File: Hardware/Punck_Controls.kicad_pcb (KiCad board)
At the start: 2 copper layers, 91.2 x 110 mm, 36 parts, among them J1 Conn_01x12_Female, J10 Kick_In, J11 USB_B_Micro, J12 Tempo_Out, J13 Audio_Out_L, J14 Audio_Out_R, J15 Midi_In, J2 Conn_01x12_Female, J3 Conn_01x12_Female, J4 Conn_01x12_Female, J5 Snare_In, J6 CH_In, J7 OH_In, J8 SamplerA_In, J9 SamplerB_In

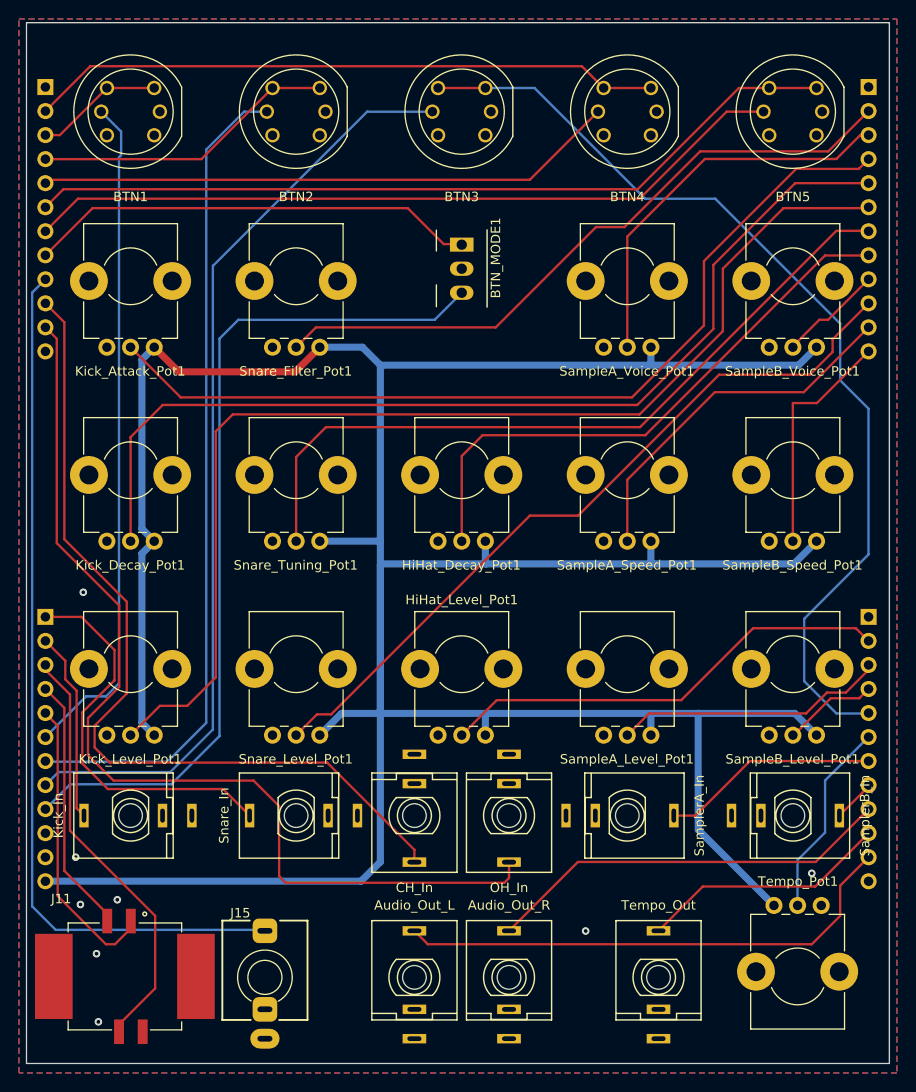
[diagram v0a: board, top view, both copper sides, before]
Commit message: Added test code to use PWM control on voice LEDs
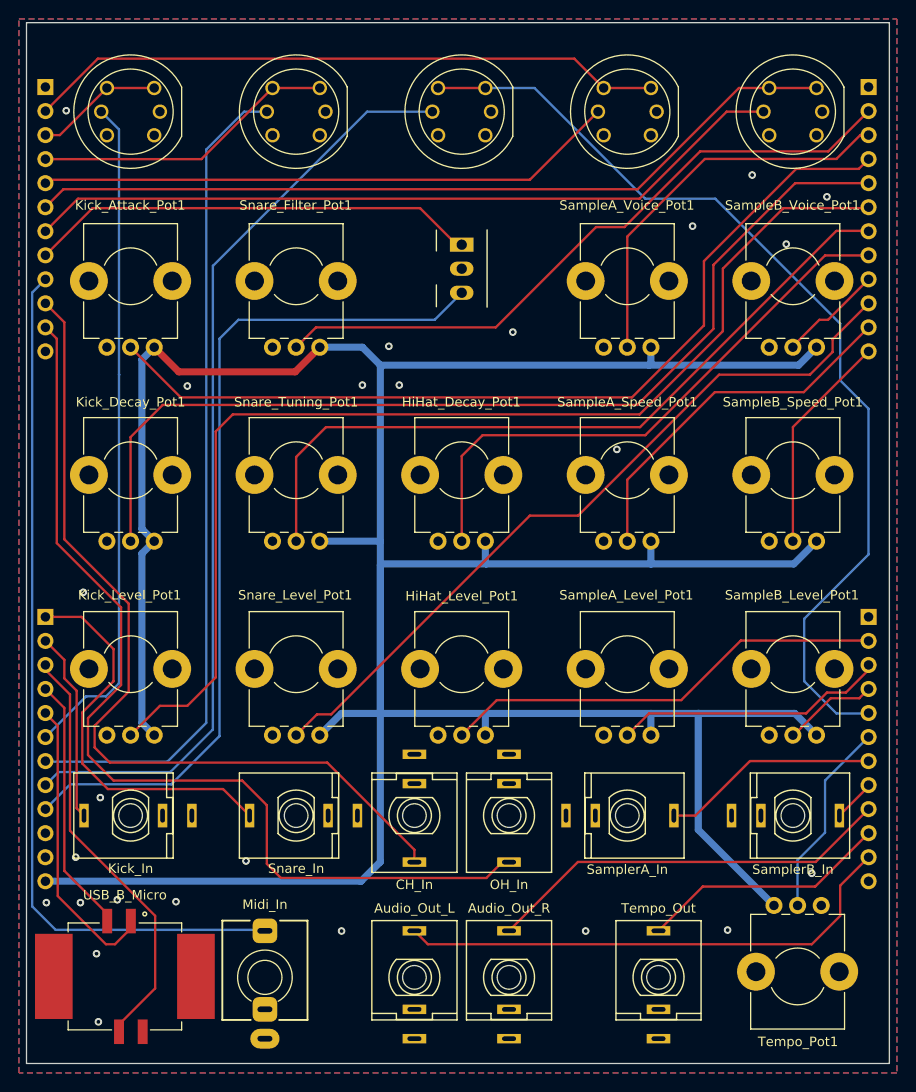
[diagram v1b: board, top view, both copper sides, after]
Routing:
- net /OH_IN: track 106.1 -> 104.2 mm
- net /SAMPLER_B_SPEED_POT: track 24.9 -> 23.4 mm
- net /HIHAT_VOL_POT: track 48.2 -> 47.2 mm
- net /SA_BTN: track 66.9 -> 67.6 mm
- net GND: vias 8 -> 25

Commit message: Final tweaking and v1 gerber creation; JLC order placed
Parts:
- moved J10 0.89 mm to (80.6, 133.0)
- moved J12 0.89 mm to (136.4, 150.1)
- moved J13 0.89 mm to (110.6, 150.1)
- moved J14 0.89 mm to (120.6, 150.1)
- moved J5 0.89 mm to (98.1, 133.0)
- moved J6 0.89 mm to (110.6, 133.0)
- moved J7 0.89 mm to (120.6, 133.0)
- moved J8 0.89 mm to (133.1, 133.0)
- moved J9 0.89 mm to (150.6, 133.0)
- moved Tempo_Pot1 0.89 mm to (151.1, 150.0)
- moved BTN1 0.89 mm to (80.6, 58.6)
- moved BTN2 0.89 mm to (98.1, 58.6)
- moved BTN3 0.89 mm to (115.6, 58.6)
- moved BTN4 0.89 mm to (133.1, 58.6)
- moved BTN5 0.89 mm to (150.6, 58.6)
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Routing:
- net /USB_DM: track 27.2 -> 32.1 mm
- net /USB_VBUS: track 31.1 -> 27.3 mm
- net /USB_DP: track 45.9 -> 44.5 mm
- net /SAMPLER_B_IN: track 4.50 -> 5.28 mm
- net /OH_IN: track 104.2 -> 104.7 mm
- net /SN_LED: track 87.4 -> 86.9 mm
- net /HH_LED: track 99.1 -> 98.6 mm
- net /KI_BTN: track 13.6 -> 13.1 mm
- net /SN_BTN: track 32.1 -> 31.6 mm
- net GND: vias 25 -> 38
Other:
- board text added: "Hihat"
- board text added: "Kick"
- board text added: "Mountjoy Modular Punck Controls v1.0"
- board text added: "Sample A"
- board text added: "Sample B"
- board text added: "Snare"
